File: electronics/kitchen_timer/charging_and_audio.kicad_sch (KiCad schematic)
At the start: 5 parts, among them J1 JST_2pin_2.5mm, Q5 BC337

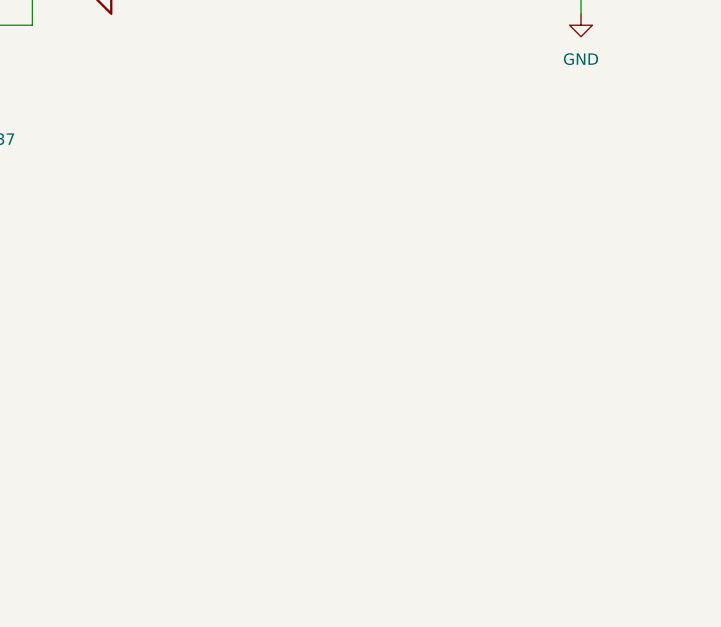
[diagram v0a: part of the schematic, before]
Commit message: Add 3d models to components, small rerouting
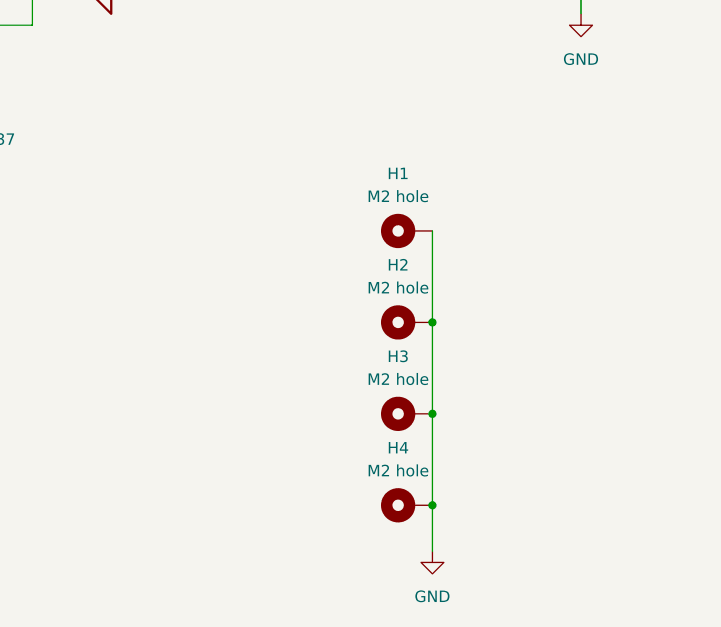
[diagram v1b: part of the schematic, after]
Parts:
- added H1, H2, H3, H4: M2 hole, MountingHole:MountingHole_2.2mm_M2_Pad_Via, symbol Mechanical:MountingHole_Pad
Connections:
- net GND: now also H1.1, H2.1, H3.1, H4.1

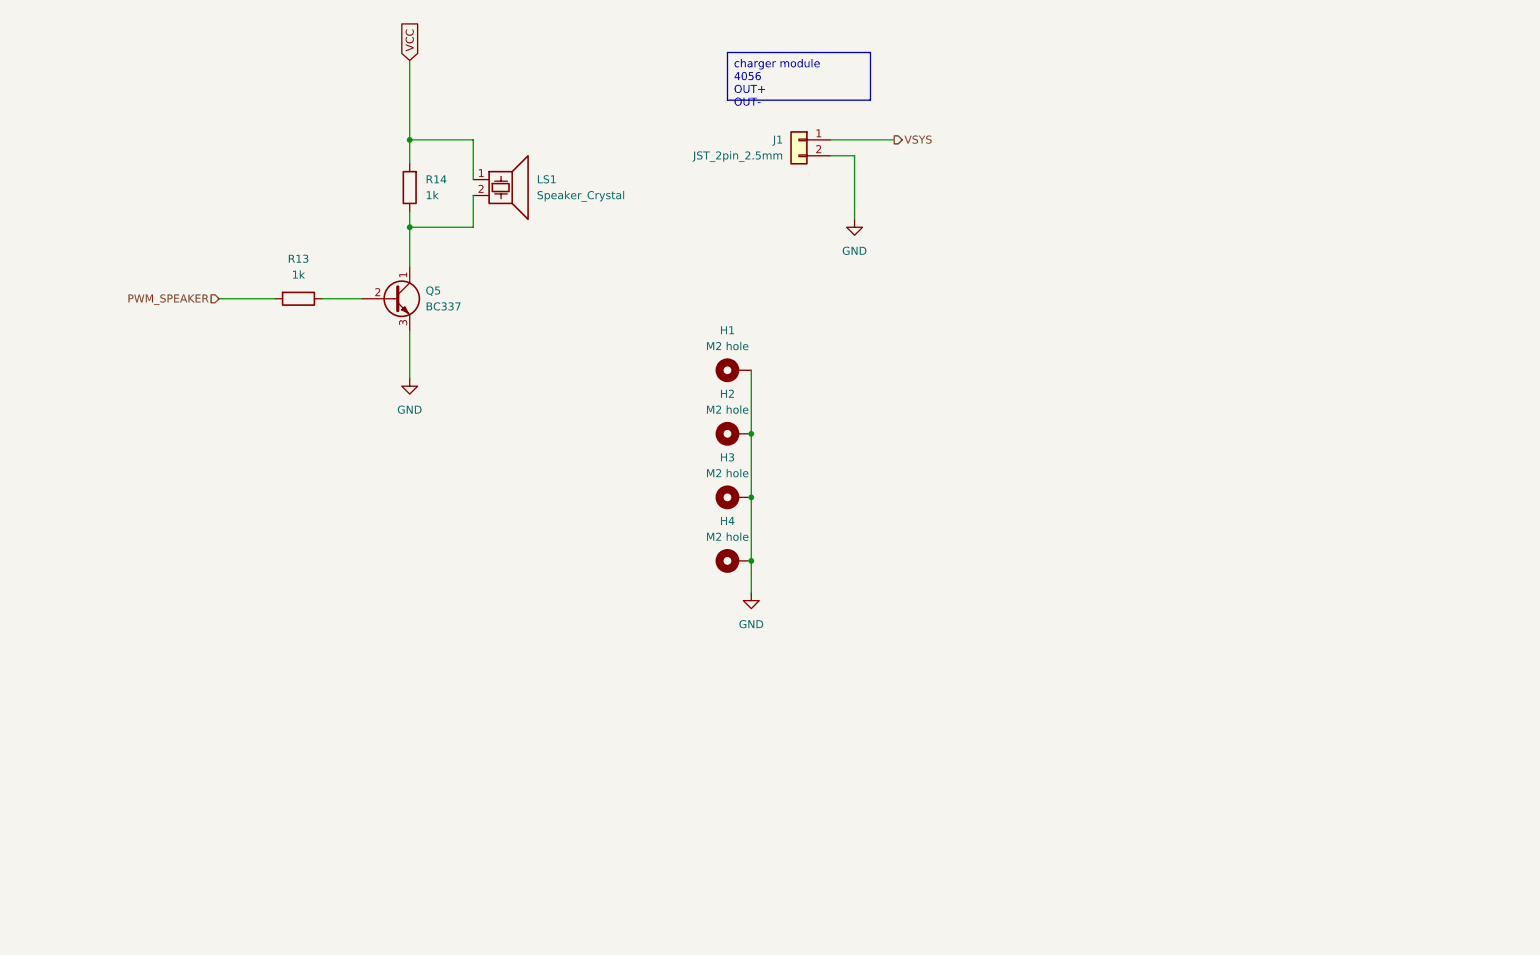
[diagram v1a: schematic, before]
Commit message: Update electronics
- added Schottky diode and solder bridge
- corrected all errors from design rules checker
- added silk screen logos
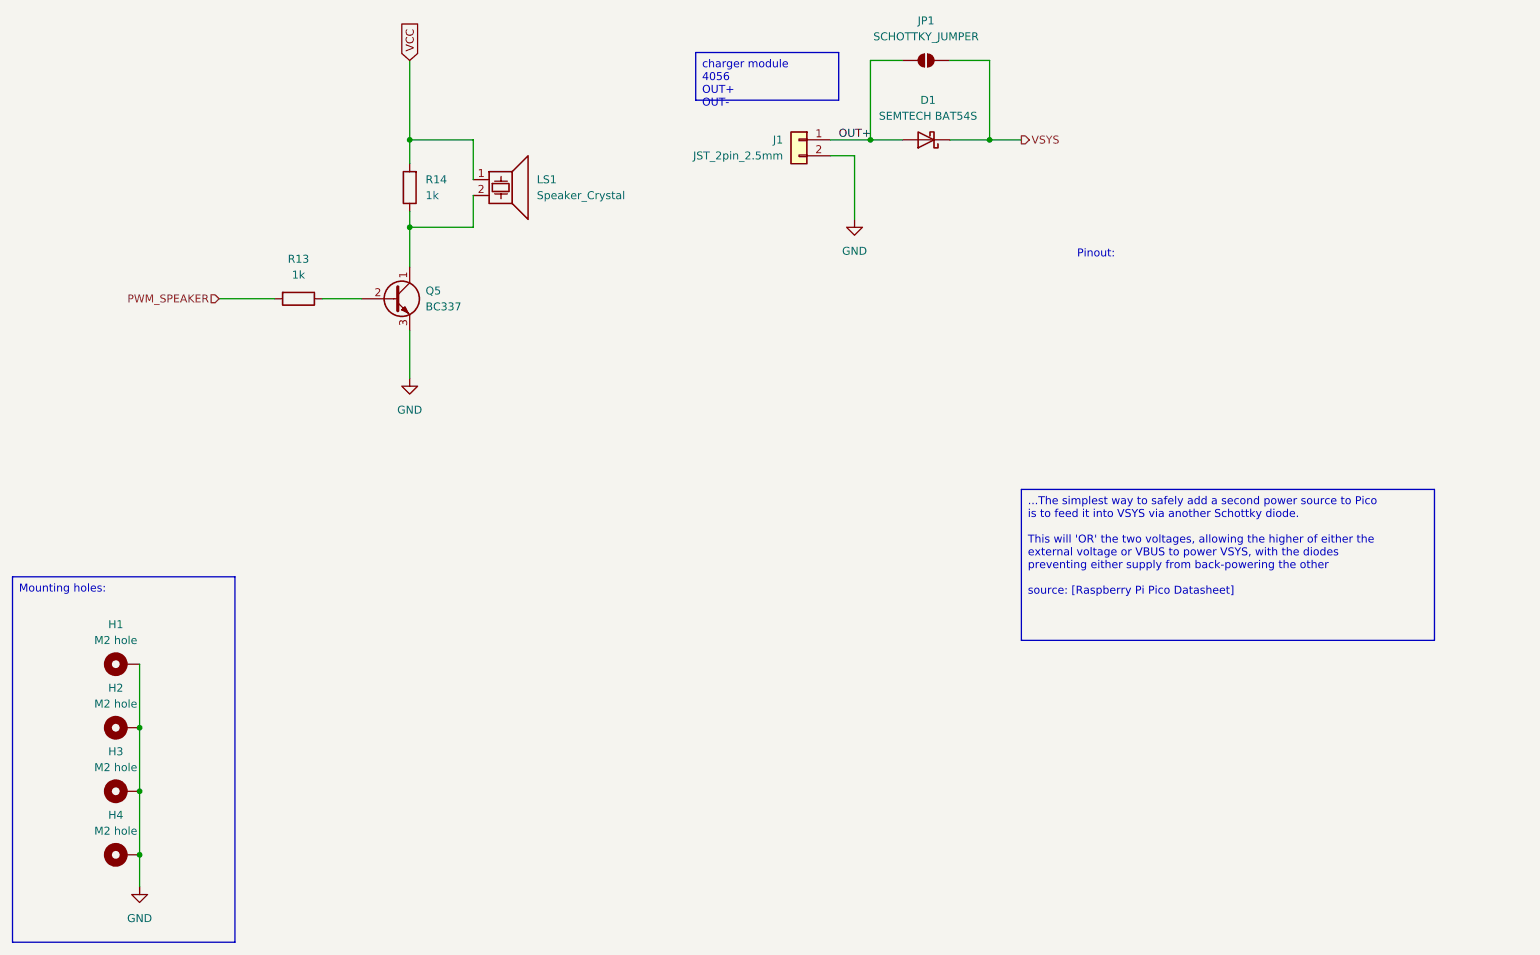
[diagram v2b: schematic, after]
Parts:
- added D1: SEMTECH BAT54S, Package_TO_SOT_SMD:TSOT-23, symbol Device:D_Schottky
- added JP1: SCHOTTKY_JUMPER, Jumper:SolderJumper-2_P1.3mm_Open_Pad1.0x1.5mm, symbol Jumper:SolderJumper_2_Open
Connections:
- net VSYS: now also D1.1 (K), JP1.2 (B); no longer J1.1 (Pin_1)
- new net OUT+: D1.2 (A), J1.1 (Pin_1), JP1.1 (A)
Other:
- note added: "Pinout:"
- moved on the sheet: H1, H2, H3, H4

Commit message: Update electronics
- resistors with longer spacing between holes
- GND for SWD
- solder jumper new footprint
- increase distances between nets

- added datasheet for schottky
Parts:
- D1: footprint Package_TO_SOT_SMD:TSOT-23 -> Custom_footprints:SOT-23_Handsoldering_renumbered
- JP1: footprint Jumper:SolderJumper-2_P1.3mm_Open_Pad1.0x1.5mm -> Jumper:SolderJumper-2_P1.3mm_Open_TrianglePad1.0x1.5mm
- R13, R14: footprint Resistor_THT:R_Axial_DIN0207_L6.3mm_D2.5mm_P7.62mm_Horizontal -> Resistor_THT:R_Axial_DIN0207_L6.3mm_D2.5mm_P10.16mm_Horizontal
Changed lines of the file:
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@@
 			)
 		)
-		(property "Footprint" "Resistor_THT:R_Axial_DIN0207_L6.3mm_D2.5mm_P7.62mm_Horizontal"
+		(property "Footprint" "Resistor_THT:R_Axial_DIN0207_L6.3mm_D2.5mm_P10.16mm_Horizontal"
 			(at 76.2 76.962 90)
 			(effects
@@
 			)
 		)
-		(property "Footprint" "Package_TO_SOT_SMD:TSOT-23"
+		(property "Footprint" "Custom_footprints:SOT-23_Handsoldering_renumbered"
 			(at 176.53 53.34 0)
 			(effects
@@
 			)
 		)
-		(property "Footprint" "Resistor_THT:R_Axial_DIN0207_L6.3mm_D2.5mm_P7.62mm_Horizontal"
+		(property "Footprint" "Resistor_THT:R_Axial_DIN0207_L6.3mm_D2.5mm_P10.16mm_Horizontal"
 			(at 95.758 60.96 90)
 			(effects
@@
 			)
 		)
-		(property "Footprint" "Jumper:SolderJumper-2_P1.3mm_Open_Pad1.0x1.5mm"
+		(property "Footprint" "Jumper:SolderJumper-2_P1.3mm_Open_TrianglePad1.0x1.5mm"
 			(at 176.53 40.64 0)
 			(effects
